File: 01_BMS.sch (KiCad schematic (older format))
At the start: 37 parts

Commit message: LDO für Audio DSP hinzugefügt
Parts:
- removed R? (x2): ?, symbol Device:R_Small
- added Q?: Q_NMOS_DGS, symbol Device:Q_NMOS_DGS
- added R?: 100R, symbol Device:R_Small
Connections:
- net labels added: DISCHARGE_LOAD, PACK+
- net labels removed: CHARGE_PACK+, DISCHARGE_PACK+
- wire segments 134 -> 137
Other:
- note added: "To voltage devider"
- moved on the sheet: C?, R?, U?

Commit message: 3v3 über LDO von BMS enablen. Bluetooth hinzugefügt
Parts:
- added R?: 10K, symbol Device:R_Small
- gave numbers to parts that had none: 37
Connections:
- net labels added: BATTERY+
- net labels removed: +BATTERY
- wire segments 137 -> 143

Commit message: Schaltplan fertig. Fertig für review
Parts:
- added D?: SS16HE, symbol Device:D_Small
- added R? (x3): 10K, symbol Device:R_Small
- added R? (x3): 100K, symbol Device:R_Small
- added R? (x2): xx, symbol Device:R_Small
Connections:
- net labels added: PACK_VOLTAGE
- net labels removed: PACKDIV
- wire segments 143 -> 153
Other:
- moved on the sheet: C213, C214, C215, R212, R213, R214, R215, R216, R?, U202

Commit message: Footprintzuordnung angefangen
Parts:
- C201, C202, C203, C204, C205, C206, C207, C208, C209, C210, C211, C213, C214, C215: footprint (none) -> Capacitor_SMD:C_0603_1608Metric_Pad1.05x0.95mm_HandSolder
- C212: footprint (none) -> Capacitor_SMD:CP_Elec_6.3x5.9
- gave numbers to parts that had none: 10
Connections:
- net labels added: +BATT
- net labels removed: LDO_BQ76920
- wire segments 153 -> 155
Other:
- note added: "LDO_Output"
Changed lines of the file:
@@
 F 0 "C201" H 3292 2596 50  0000 L CNN
 F 1 "1uF" H 3292 2505 50  0000 L CNN
-F 2 "" H 3200 2550 50  0001 C CNN
+F 2 "Capacitor_SMD:C_0603_1608Metric_Pad1.05x0.95mm_HandSolder" H 3200 2550 50  0001 C CNN
 F 3 "~" H 3200 2550 50  0001 C CNN
 	1    3200 2550
@@
 F 0 "C202" H 3292 3096 50  0000 L CNN
 F 1 "1uF" H 3292 3005 50  0000 L CNN
-F 2 "" H 3200 3050 50  0001 C CNN
+F 2 "Capacitor_SMD:C_0603_1608Metric_Pad1.05x0.95mm_HandSolder" H 3200 3050 50  0001 C CNN
 F 3 "~" H 3200 3050 50  0001 C CNN
 	1    3200 3050
@@
 F 0 "C205" H 3292 4096 50  0000 L CNN
 F 1 "1uF" H 3292 4005 50  0000 L CNN
-F 2 "" H 3200 4050 50  0001 C CNN
+F 2 "Capacitor_SMD:C_0603_1608Metric_Pad1.05x0.95mm_HandSolder" H 3200 4050 50  0001 C CNN
 F 3 "~" H 3200 4050 50  0001 C CNN
 	1    3200 4050
@@
 F 0 "C203" H 3292 3596 50  0000 L CNN
 F 1 "1uF" H 3292 3505 50  0000 L CNN
-F 2 "" H 3200 3550 50  0001 C CNN
+F 2 "Capacitor_SMD:C_0603_1608Metric_Pad1.05x0.95mm_HandSolder" H 3200 3550 50  0001 C CNN
 F 3 "~" H 3200 3550 50  0001 C CNN
 	1    3200 3550
@@
 F 0 "C204" H 3292 3896 50  0000 L CNN
 F 1 "1uF" H 3292 3805 50  0000 L CNN
-F 2 "" H 3200 3850 50  0001 C CNN
+F 2 "Capacitor_SMD:C_0603_1608Metric_Pad1.05x0.95mm_HandSolder" H 3200 3850 50  0001 C CNN
 F 3 "~" H 3200 3850 50  0001 C CNN
 	1    3200 3850
@@
 F 0 "C209" V 4321 2500 50  0000 C CNN
 F 1 "10uF" V 4412 2500 50  0000 C CNN
-F 2 "" H 4550 2500 50  0001 C CNN
+F 2 "Capacitor_SMD:C_0603_1608Metric_Pad1.05x0.95mm_HandSolder" H 4550 2500 50  0001 C CNN
 F 3 "~" H 4550 2500 50  0001 C CNN
 	1    4550 2500
@@
 F 0 "C210" H 4858 4254 50  0000 R CNN
 F 1 "1uF" H 4858 4345 50  0000 R CNN
-F 2 "" H 4950 4300 50  0001 C CNN
+F 2 "Capacitor_SMD:C_0603_1608Metric_Pad1.05x0.95mm_HandSolder" H 4950 4300 50  0001 C CNN
 F 3 "~" H 4950 4300 50  0001 C CNN
 	1    4950 4300
@@
 F 0 "C207" V 3921 4500 50  0000 C CNN
 F 1 "0.1uF" V 4012 4500 50  0000 C CNN
-F 2 "" H 4150 4500 50  0001 C CNN
+F 2 "Capacitor_SMD:C_0603_1608Metric_Pad1.05x0.95mm_HandSolder" H 4150 4500 50  0001 C CNN
 F 3 "~" H 4150 4500 50  0001 C CNN
 	1    4150 4500
@@
 F 0 "C206" V 3621 4500 50  0000 C CNN
 F 1 "0.1uF" V 3712 4500 50  0000 C CNN
-F 2 "" H 3850 4500 50  0001 C CNN
+F 2 "Capacitor_SMD:C_0603_1608Metric_Pad1.05x0.95mm_HandSolder" H 3850 4500 50  0001 C CNN
 F 3 "~" H 3850 4500 50  0001 C CNN
 	1    3850 4500
@@
 F 0 "C208" V 4221 4500 50  0000 C CNN
 F 1 "0.1uF" V 4312 4500 50  0000 C CNN
-F 2 "" H 4450 4500 50  0001 C CNN
+F 2 "Capacitor_SMD:C_0603_1608Metric_Pad1.05x0.95mm_HandSolder" H 4450 4500 50  0001 C CNN
 F 3 "~" H 4450 4500 50  0001 C CNN
 	1    4450 4500
@@
 F 0 "C211" H 5308 2204 50  0000 R CNN
 F 1 "1uF" H 5308 2295 50  0000 R CNN
-F 2 "" H 5400 2250 50  0001 C CNN
+F 2 "Capacitor_SMD:C_0603_1608Metric_Pad1.05x0.95mm_HandSolder" H 5400 2250 50  0001 C CNN
 F 3 "~" H 5400 2250 50  0001 C CNN
 	1    5400 2250
@@
 F 0 "C212" H 5758 3004 50  0000 R CNN
 F 1 "4.7uF" H 5758 3095 50  0000 R CNN
-F 2 "" H 5850 3050 50  0001 C CNN
+F 2 "Capacitor_SMD:CP_Elec_6.3x5.9" H 5850 3050 50  0001 C CNN
 F 3 "~" H 5850 3050 50  0001 C CNN
 	1    5850 3050
@@
 	0    -1   -1   0
 $EndComp
-Text GLabel 6600 3150 2    50   Output ~ 0
-LDO_BQ76920
-Connection ~ 5850 3150
 $Comp
 L Device:R_Small R211
@@
 R_Therm
 Wire Wire Line
-	5850 3150 6600 3150
-Wire Wire Line
 	5600 3300 5650 3300
 Wire Wire Line
@@
 F 0 "C215" H 8042 2746 50  0000 L CNN
 F 1 "10nF" H 8042 2655 50  0000 L CNN
-F 2 "" H 7950 2700 50  0001 C CNN
+F 2 "Capacitor_SMD:C_0603_1608Metric_Pad1.05x0.95mm_HandSolder" H 7950 2700 50  0001 C CNN
 F 3 "~" H 7950 2700 50  0001 C CNN
 	1    7950 2700
@@
 F 0 "C214" H 7642 2746 50  0000 L CNN
 F 1 "470nF" H 7642 2655 50  0000 L CNN
-F 2 "" H 7550 2700 50  0001 C CNN
+F 2 "Capacitor_SMD:C_0603_1608Metric_Pad1.05x0.95mm_HandSolder" H 7550 2700 50  0001 C CNN
 F 3 "~" H 7550 2700 50  0001 C CNN
 	1    7550 2700
@@
 F 0 "C213" V 10521 3450 50  0000 C CNN
 F 1 "10nF" V 10612 3450 50  0000 C CNN
-F 2 "" H 10750 3450 50  0001 C CNN
+F 2 "Capacitor_SMD:C_0603_1608Metric_Pad1.05x0.95mm_HandSolder" H 10750 3450 50  0001 C CNN
 F 3 "~" H 10750 3450 50  0001 C CNN
 	1    10750 3450
@@
 $EndComp
 Wire Wire Line
-	7100 4800 4300 4800
+	7100 4800 6850 4800
 Connection ~ 4300 4800
 Text Label 1650 3250 0    50   ~ 0
@@
 Connection ~ 6400 2150
 $Comp
-L Device:R_Small R?
+L Device:R_Small R217
 U 1 1 5E8D7080
 P 6150 2750
-F 0 "R?" V 6050 2700 50  0000 C CNN
+F 0 "R217" V 6050 2700 50  0000 C CNN
 F 1 "10K" V 6050 2850 50  0000 C CNN
 F 2 "" H 6150 2750 50  0001 C CNN
@@
 	2300 3450 2300 3750
 $Comp
-L Device:D_Small D?
+L Device:D_Small D201
 U 1 1 5ED09080
 P 6500 2750
-F 0 "D?" H 6500 2955 50  0000 C CNN
+F 0 "D201" H 6500 2955 50  0000 C CNN
 F 1 "SS16HE" H 6500 2864 50  0000 C CNN
 F 2 "" V 6500 2750 50  0001 C CNN
@@
 	6400 2750 6250 2750
 $Comp
-L Device:R_Small R?
+L Device:R_Small R221
 U 1 1 5ED70E97
 P 9300 3700
-F 0 "R?" V 9250 3800 50  0000 C CNN
+F 0 "R221" V 9250 3800 50  0000 C CNN
 F 1 "10K" V 9250 3550 50  0000 C CNN
 F 2 "" H 9300 3700 50  0001 C CNN
@@
 $EndComp
 $Comp
-L Device:R_Small R?
+L Device:R_Small R223
 U 1 1 5ED71182
 P 9550 3800
-F 0 "R?" V 9500 3900 50  0000 C CNN
+F 0 "R223" V 9500 3900 50  0000 C CNN
 F 1 "10K" V 9500 3650 50  0000 C CNN
 F 2 "" H 9550 3800 50  0001 C CNN
@@
 $EndComp
 $Comp
-L Device:R_Small R?
+L Device:R_Small R225
 U 1 1 5ED711F0
 P 9800 3900
-F 0 "R?" V 9750 4000 50  0000 C CNN
+F 0 "R225" V 9750 4000 50  0000 C CNN
 F 1 "10K" V 9750 3750 50  0000 C CNN
 F 2 "" H 9800 3900 50  0001 C CNN
@@
 	10050 3900 9900 3900
 $Comp
-L Device:R_Small R?
+L Device:R_Small R220
 U 1 1 5ED8E261
 P 9200 4450
-F 0 "R?" V 9100 4300 50  0000 R CNN
+F 0 "R220" V 9100 4300 50  0000 R CNN
 F 1 "100K" V 9100 4550 50  0000 R CNN
 F 2 "" H 9200 4450 50  0001 C CNN
@@
 $EndComp
 $Comp
-L Device:R_Small R?
+L Device:R_Small R222
 U 1 1 5ED8E4D8
 P 9450 4450
-F 0 "R?" V 9350 4300 50  0000 R CNN
+F 0 "R222" V 9350 4300 50  0000 R CNN
 F 1 "100K" V 9350 4550 50  0000 R CNN
 F 2 "" H 9450 4450 50  0001 C CNN
@@
 $EndComp
 $Comp
-L Device:R_Small R?
+L Device:R_Small R224
 U 1 1 5ED8E550
 P 9700 4450
-F 0 "R?" V 9600 4300 50  0000 R CNN
+F 0 "R224" V 9600 4300 50  0000 R CNN
 F 1 "100K" V 9600 4550 50  0000 R CNN
 F 2 "" H 9700 4450 50  0001 C CNN
@@
 	9700 3900 8900 3900
 $Comp
-L power:GND #PWR?
+L power:GND #PWR0202
 U 1 1 5ED9E8D5
 P 9200 4550
-F 0 "#PWR?" H 9200 4300 50  0001 C CNN
+F 0 "#PWR0202" H 9200 4300 50  0001 C CNN
 F 1 "GND" H 9205 4377 50  0000 C CNN
 F 2 "" H 9200 4550 50  0001 C CNN
@@
 $EndComp
 $Comp
-L power:GND #PWR?
+L power:GND #PWR0203
 U 1 1 5ED9E9CB
 P 9450 4550
-F 0 "#PWR?" H 9450 4300 50  0001 C CNN
+F 0 "#PWR0203" H 9450 4300 50  0001 C CNN
 F 1 "GND" H 9455 4377 50  0000 C CNN
 F 2 "" H 9450 4550 50  0001 C CNN
@@
 $EndComp
 $Comp
-L power:GND #PWR?
+L power:GND #PWR0204
 U 1 1 5ED9EA30
 P 9700 4550
-F 0 "#PWR?" H 9700 4300 50  0001 C CNN
+F 0 "#PWR0204" H 9700 4300 50  0001 C CNN
 F 1 "GND" H 9705 4377 50  0000 C CNN
 F 2 "" H 9700 4550 50  0001 C CNN
@@
 	8900 3700 9200 3700
 $Comp
-L Device:R_Small R?
+L Device:R_Small R218
 U 1 1 5EDF6B57
 P 8950 4450
-F 0 "R?" V 8850 4300 50  0000 R CNN
+F 0 "R218" V 8850 4300 50  0000 R CNN
 F 1 "xx" V 8850 4550 50  0000 R CNN
 F 2 "" H 8950 4450 50  0001 C CNN
@@
 $EndComp
 $Comp
-L Device:R_Small R?
+L Device:R_Small R219
 U 1 1 5EDF6BD1
 P 8950 5150
-F 0 "R?" V 8850 5000 50  0000 R CNN
+F 0 "R219" V 8850 5000 50  0000 R CNN
 F 1 "xx" V 8850 5250 50  0000 R CNN
 F 2 "" H 8950 5150 50  0001 C CNN
@@
 	8950 4850 8950 5050
 $Comp
-L power:GND #PWR?
+L power:GND #PWR0201
 U 1 1 5EE06B27
 P 8950 5250
-F 0 "#PWR?" H 8950 5000 50  0001 C CNN
+F 0 "#PWR0201" H 8950 5000 50  0001 C CNN
 F 1 "GND" H 8955 5077 50  0000 C CNN
 F 2 "" H 8950 5250 50  0001 C CNN
@@
 	6400 2150 7950 2150
 Wire Wire Line
-	5400 2150 6400 2150
+	5400 2150 5750 2150
 Wire Wire Line
 	10650 2950 10650 2150
@@
 Wire Wire Line
 	8900 3450 10650 3450
+$Comp
+L power:+BATT #PWR0176
+U 1 1 5EAE2603
+P 6100 2150
+F 0 "#PWR0176" H 6100 2000 50  0001 C CNN
+F 1 "+BATT" H 6115 2323 50  0000 C CNN
+F 2 "" H 6100 2150 50  0001 C CNN
+F 3 "" H 6100 2150 50  0001 C CNN
+	1    6100 2150
+	1    0    0    -1
+$EndComp
+Connection ~ 6100 2150
+Wire Wire Line
+	6100 2150 6400 2150
+$Comp
+L power:PWR_FLAG #FLG0102
+U 1 1 5EB62017
+P 5750 2150
+F 0 "#FLG0102" H 5750 2225 50  0001 C CNN
+F 1 "PWR_FLAG" H 5750 2324 50  0000 C CNN
+F 2 "" H 5750 2150 50  0001 C CNN
+F 3 "~" H 5750 2150 50  0001 C CNN
+	1    5750 2150
+	1    0    0    -1
+$EndComp
+Connection ~ 5750 2150
+Wire Wire Line
+	5750 2150 6100 2150
+$Comp
+L power:PWR_FLAG #FLG0104
+U 1 1 5EB6DC0C
+P 8250 2550
+F 0 "#FLG0104" H 8250 2625 50  0001 C CNN
+F 1 "PWR_FLAG" H 8350 2700 50  0000 C CNN
+F 2 "" H 8250 2550 50  0001 C CNN
+F 3 "~" H 8250 2550 50  0001 C CNN
+	1    8250 2550
+	1    0    0    -1
+$EndComp
+Connection ~ 8250 2550
+Text Notes 6250 3150 0    50   ~ 0
+LDO_Output
+$Comp
+L power:PWR_FLAG #FLG0107
+U 1 1 5EB892DF
+P 6850 4800
+F 0 "#FLG0107" H 6850 4875 50  0001 C CNN
+F 1 "PWR_FLAG" H 6850 4974 50  0000 C CNN
+F 2 "" H 6850 4800 50  0001 C CNN
+F 3 "~" H 6850 4800 50  0001 C CNN
+	1    6850 4800
+	1    0    0    -1
+$EndComp
+Connection ~ 6850 4800
+Wire Wire Line
+	6850 4800 4300 4800
 $EndSCHEMATC

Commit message: fast alle footprints herausgesucht. Spulen typen rausgesucht: Bourns spulen
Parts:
- removed Q201, Q202, Q203: Q_NMOS_DGS, symbol Device:Q_NMOS_DGS
- added Q201, Q202, Q203: NTD14N03RT4G, Package_TO_SOT_SMD:TO-263-2, symbol Device:Q_NMOS_GDS
- D201: footprint (none) -> Diode_SMD:D_SOD-323
- J201: value Screw_Terminal_01x07 -> TB001-500-07BE CUI_Devices; footprint (none) -> TerminalBlock_RND:TerminalBlock_RND_205-00050_1x07_P5.00mm_Horizontal
- R201, R202, R203, R204, R205, R206, R208, R209, R210, R211, R212, R213, R214, R216, R217, R218, R219, R220, R221, R222, R223, R224, R225: footprint (none) -> Resistor_SMD:R_0603_1608Metric_Pad1.05x0.95mm_HandSolder
- R207: value 0.01R -> 0.01R PCS1206DR0100ET; footprint (none) -> Resistor_SMD:R_1206_3216Metric_Pad1.42x1.75mm_HandSolder
- R215: footprint (none) -> Resistor_SMD:R_1206_3216Metric_Pad1.42x1.75mm_HandSolder
- U201: footprint (none) -> Package_SO:TSSOP-20_4.4x6.5mm_P0.65mm
- U202: footprint (none) -> Package_SO:TSSOP-16_4.4x5mm_P0.65mm
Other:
- note added: "<--- Charge Batterie"
- note added: "<--- Discharge Capacitor Load"
- note added: "Discharge Batterie--->"
- moved on the sheet: R215

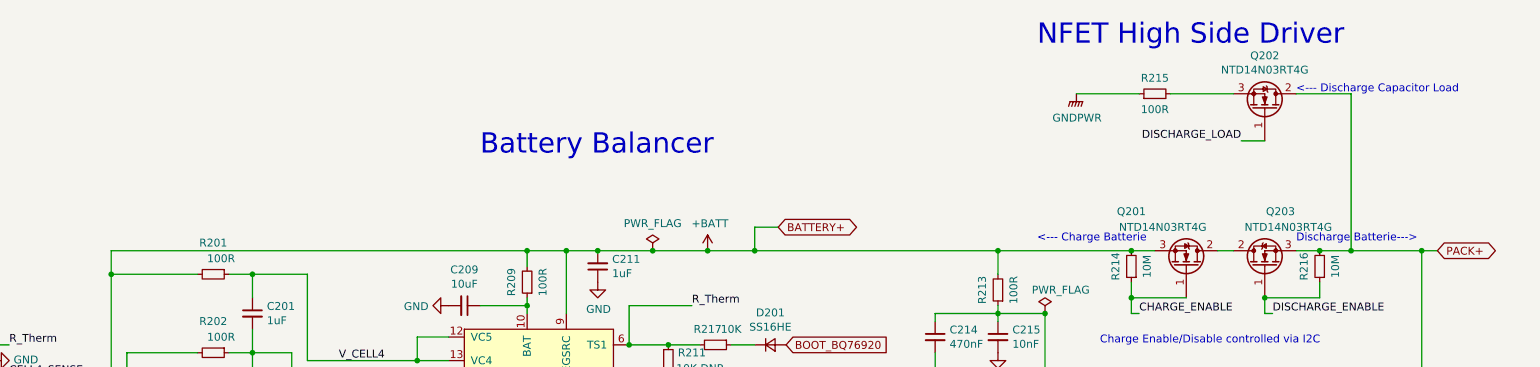
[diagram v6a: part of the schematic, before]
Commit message: Mountingholes und Heatsinks hinzugefügt
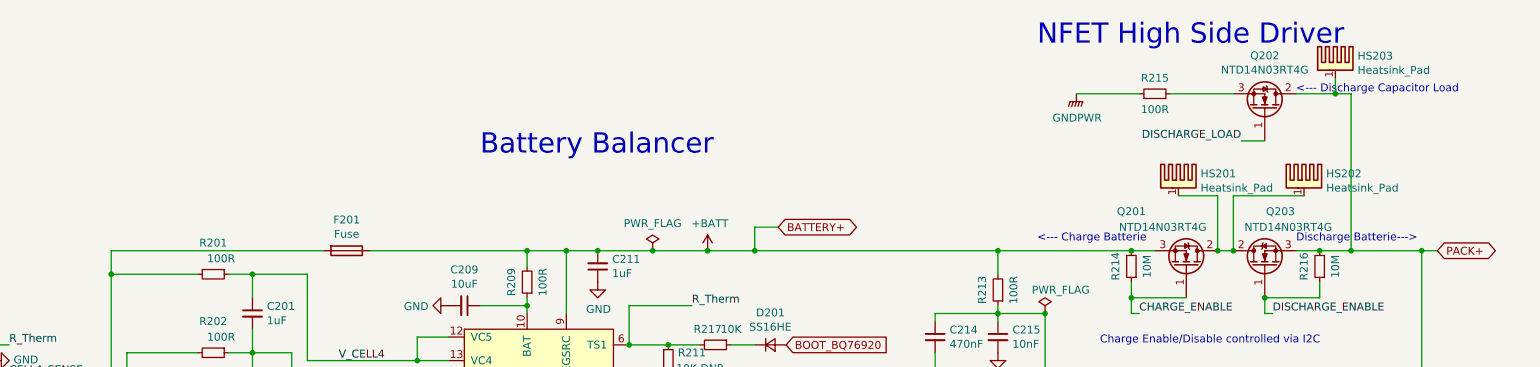
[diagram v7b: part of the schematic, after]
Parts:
- added F201: Fuse, Fuse:Fuseholder_Cylinder-5x20mm_Schurter_0031_8201_Horizontal_Open, symbol Device:Fuse
- added HS201, HS202, HS203: Heatsink_Pad, Heatsink:Heatsink_AAVID_573300D00010G_TO-263, symbol Mechanical:Heatsink_Pad
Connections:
- net +BATT: now also F201.1; no longer J201.5 (Pin_5), R201.2
- net PACK+: now also HS203.1
- net at Q201.2 (D), Q203.2 (D): now also HS201.1, HS202.1
- new net CELL4_SENSE: F201.2, J201.5 (Pin_5), R201.2
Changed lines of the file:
@@
 	2300 2150 2300 2300
 Connection ~ 2300 2300
-Wire Wire Line
-	2300 2150 4950 2150
 $Comp
 L Device:R_Small R209
@@
 	5400 2150 5200 2150
 Connection ~ 5400 2150
-Connection ~ 4950 2150
 Wire Wire Line
 	5200 2550 5200 2150
@@
 	10200 1150 10200 2150
 Wire Wire Line
-	9850 1150 10200 1150
+	9850 1150 10100 1150
 Connection ~ 10200 2150
 Wire Wire Line
@@
 Text Notes 9850 2100 0    50   ~ 0
 Discharge Batterie--->
+$Comp
+L Device:Fuse F201
+U 1 1 5E961D10
+P 3800 2150
+F 0 "F201" V 3603 2150 50  0000 C CNN
+F 1 "Fuse" V 3694 2150 50  0000 C CNN
+F 2 "Fuse:Fuseholder_Cylinder-5x20mm_Schurter_0031_8201_Horizontal_Open" V 3730 2150 50  0001 C CNN
+F 3 "https://www.mouser.de/datasheet/2/358/typ_OGN-14523.pdf" H 3800 2150 50  0001 C CNN
+	1    3800 2150
+	0    1    1    0
+$EndComp
+Wire Wire Line
+	4950 2150 3950 2150
+Connection ~ 4950 2150
+Wire Wire Line
+	3650 2150 2300 2150
+$Comp
+L Mechanical:Heatsink_Pad HS?
+U 1 1 5E9AC02A
+P 10100 950
+AR Path="/5E73BAE8/5E9AC02A" Ref="HS?"  Part="1"
+AR Path="/5E73BADE/5E9AC02A" Ref="HS203"  Part="1"
+F 0 "HS203" H 10241 991 50  0000 L CNN
+F 1 "Heatsink_Pad" H 10241 900 50  0000 L CNN
+F 2 "Heatsink:Heatsink_AAVID_573300D00010G_TO-263" H 10112 900 50  0001 C CNN
+F 3 "~" H 10112 900 50  0001 C CNN
+	1    10100 950
+	1    0    0    -1
+$EndComp
+Wire Wire Line
+	10100 1150 10100 1050
+Connection ~ 10100 1150
+Wire Wire Line
+	10100 1150 10200 1150
+$Comp
+L Mechanical:Heatsink_Pad HS?
+U 1 1 5E9B8E57
+P 9100 1700
+AR Path="/5E73BAE8/5E9B8E57" Ref="HS?"  Part="1"
+AR Path="/5E73BADE/5E9B8E57" Ref="HS201"  Part="1"
+F 0 "HS201" H 9241 1741 50  0000 L CNN
+F 1 "Heatsink_Pad" H 9241 1650 50  0000 L CNN
+F 2 "Heatsink:Heatsink_AAVID_573300D00010G_TO-263" H 9112 1650 50  0001 C CNN
+F 3 "~" H 9112 1650 50  0001 C CNN
+	1    9100 1700
+	1    0    0    -1
+$EndComp
+$Comp
+L Mechanical:Heatsink_Pad HS?
+U 1 1 5E9BEE65
+P 9900 1700
+AR Path="/5E73BAE8/5E9BEE65" Ref="HS?"  Part="1"
+AR Path="/5E73BADE/5E9BEE65" Ref="HS202"  Part="1"
+F 0 "HS202" H 10041 1741 50  0000 L CNN
+F 1 "Heatsink_Pad" H 10041 1650 50  0000 L CNN
+F 2 "Heatsink:Heatsink_AAVID_573300D00010G_TO-263" H 9912 1650 50  0001 C CNN
+F 3 "~" H 9912 1650 50  0001 C CNN
+	1    9900 1700
+	1    0    0    -1
+$EndComp
+Wire Wire Line
+	9900 1800 9450 1800
+Wire Wire Line
+	9450 1800 9450 2150
+Connection ~ 9450 2150
+Wire Wire Line
+	9100 1800 9350 1800
+Wire Wire Line
+	9350 1800 9350 2150
+Connection ~ 9350 2150
 $EndSCHEMATC

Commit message: fertig zum routen
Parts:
- HS201, HS202, HS203: value Heatsink_Pad -> 573300D00000G
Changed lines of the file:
@@
 Text Notes 4650 1550 0    129  ~ 0
 Battery Balancer
-Text Notes 8200 850  0    129  ~ 0
+Text Notes 8300 750  0    129  ~ 0
 NFET High Side Driver
 Text GLabel 10050 3700 2    50   Input ~ 0
@@
 AR Path="/5E73BADE/5E9AC02A" Ref="HS203"  Part="1"
 F 0 "HS203" H 10241 991 50  0000 L CNN
-F 1 "Heatsink_Pad" H 10241 900 50  0000 L CNN
+F 1 "573300D00000G" H 10241 900 50  0000 L CNN
 F 2 "Heatsink:Heatsink_AAVID_573300D00010G_TO-263" H 10112 900 50  0001 C CNN
-F 3 "~" H 10112 900 50  0001 C CNN
+F 3 "https://www.mouser.de/datasheet/2/2/Aavid-Board-Level-Heatsinks-Catalog-2018-1507171.pdf" H 10112 900 50  0001 C CNN
 	1    10100 950
 	1    0    0    -1
@@
 AR Path="/5E73BAE8/5E9B8E57" Ref="HS?"  Part="1"
 AR Path="/5E73BADE/5E9B8E57" Ref="HS201"  Part="1"
-F 0 "HS201" H 9241 1741 50  0000 L CNN
-F 1 "Heatsink_Pad" H 9241 1650 50  0000 L CNN
+F 0 "HS201" H 8650 1800 50  0000 L CNN
+F 1 "573300D00000G" H 8350 1700 50  0000 L CNN
 F 2 "Heatsink:Heatsink_AAVID_573300D00010G_TO-263" H 9112 1650 50  0001 C CNN
-F 3 "~" H 9112 1650 50  0001 C CNN
+F 3 "https://www.mouser.de/datasheet/2/2/Aavid-Board-Level-Heatsinks-Catalog-2018-1507171.pdf" H 9112 1650 50  0001 C CNN
 	1    9100 1700
 	1    0    0    -1
@@
 AR Path="/5E73BADE/5E9BEE65" Ref="HS202"  Part="1"
 F 0 "HS202" H 10041 1741 50  0000 L CNN
-F 1 "Heatsink_Pad" H 10041 1650 50  0000 L CNN
+F 1 "573300D00000G" H 10041 1650 50  0000 L CNN
 F 2 "Heatsink:Heatsink_AAVID_573300D00010G_TO-263" H 9912 1650 50  0001 C CNN
-F 3 "~" H 9912 1650 50  0001 C CNN
+F 3 "https://www.mouser.de/datasheet/2/2/Aavid-Board-Level-Heatsinks-Catalog-2018-1507171.pdf" H 9912 1650 50  0001 C CNN
 	1    9900 1700
 	1    0    0    -1
